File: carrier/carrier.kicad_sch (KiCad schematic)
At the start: 34 parts, among them J1 Conn_01x14, J10 Conn_02x06_Odd_Even, J2 Conn_01x14, J3 Conn_01x14, J4 Conn_01x14, J5 Conn_02x14_Odd_Even, J6 Conn_02x14_Odd_Even, J7 Conn_02x14_Odd_Even, J8 Conn_02x14_Odd_Even, J9 Conn_02x06_Odd_Even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

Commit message: Tweaks based on tnt's feedback
Wired GPIO to PMOD1
Switch 6 IOs on PMOD to attach to a header
Add GND test point
Add alignment holes for breakout
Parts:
- added J11: Conn_01x06, Connector_PinHeader_2.54mm:PinHeader_1x06_P2.54mm_Vertical, symbol Connector_Generic:Conn_01x06
- added TP1: TestPoint, TestPoint:TestPoint_Keystone_5005-5009_Compact, symbol Connector:TestPoint
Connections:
- net GND: now also TP1.1
- net GPIO: now also J9.12 (Pin_12)
- net IO0: no longer J10.11 (Pin_11)
- net IO1: no longer J10.12 (Pin_12)
- net IO2: no longer J10.9 (Pin_9)
- net IO3: no longer J10.10 (Pin_10)
- net IO4: no longer J10.7 (Pin_7)
- net IO5: no longer J10.8 (Pin_8)
- net IO6: no longer J10.5 (Pin_5)
- net VCCD2_PDM: now also J10.5 (Pin_5); no longer J9.12 (Pin_12)
- new net USR0: J10.8 (Pin_8), J11.1 (Pin_1)
- new net USR1: J10.7 (Pin_7), J11.2 (Pin_2)
- new net USR2: J10.10 (Pin_10), J11.3 (Pin_3)
- new net USR3: J10.9 (Pin_9), J11.4 (Pin_4)
- new net USR4: J10.12 (Pin_12), J11.5 (Pin_5)
- new net USR5: J10.11 (Pin_11), J11.6 (Pin_6)
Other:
- note added: "6 USER IOS TO SELECT PINS TO SEND TO ICEBREAKER"
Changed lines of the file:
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@@
     (stroke (width 0) (type default) (color 0 0 0 0))
   )
+  (text "6 USER IOS TO SELECT PINS\nTO SEND TO ICEBREAKER" (at 46.99 185.42 0)
+    (effects (font (size 1.27 1.27)) (justify left bottom))
+  )
+  (label "USR4" (at 156.21 182.88 0)
+    (effects (font (size 1.27 1.27)) (justify left bottom))
+  )
   (label "IO0" (at 99.06 139.7 90)
     (effects (font (size 1.27 1.27)) (justify left bottom))
@@
     (effects (font (size 1.27 1.27)) (justify right bottom))
   )
-  (label "IO3" (at 156.21 180.34 0)
+  (label "USR5" (at 85.09 180.34 0)
     (effects (font (size 1.27 1.27)) (justify left bottom))
   )
@@
     (effects (font (size 1.27 1.27)) (justify left bottom))
   )
-  (label "IO4" (at 123.19 177.8 180)
-    (effects (font (size 1.27 1.27)) (justify right bottom))
+  (label "USR0" (at 156.21 177.8 0)
+    (effects (font (size 1.27 1.27)) (justify left bottom))
   )
   (label "IO3" (at 91.44 139.6682 90)
@@
     (effects (font (size 1.27 1.27)) (justify left bottom))
   )
+  (label "USR3" (at 85.09 185.42 0)
+    (effects (font (size 1.27 1.27)) (justify left bottom))
+  )
   (label "~CS" (at 156.21 151.13 0)
     (effects (font (size 1.27 1.27)) (justify left bottom))
@@
     (effects (font (size 1.27 1.27)) (justify left bottom))
   )
-  (label "IO5" (at 156.21 177.8 0)
-    (effects (font (size 1.27 1.27)) (justify left bottom))
-  )
   (label "VCCD_PDM" (at 172.72 43.18 180)
     (effects (font (size 1.27 1.27)) (justify right bottom))
@@
     (effects (font (size 1.27 1.27)) (justify right bottom))
   )
+  (label "USR3" (at 123.19 180.34 180)
+    (effects (font (size 1.27 1.27)) (justify right bottom))
+  )
   (label "IO30" (at 71.12 69.9454 270)
     (effects (font (size 1.27 1.27)) (justify right bottom))
@@
     (effects (font (size 1.27 1.27)) (justify left bottom))
   )
+  (label "GPIO" (at 156.21 156.21 0)
+    (effects (font (size 1.27 1.27)) (justify left bottom))
+  )
   (label "IO10" (at 73.66 139.6682 90)
     (effects (font (size 1.27 1.27)) (justify left bottom))
   )
-  (label "IO2" (at 123.19 180.34 180)
-    (effects (font (size 1.27 1.27)) (justify right bottom))
-  )
-  (label "IO1" (at 156.21 182.88 0)
+  (label "USR1" (at 123.19 177.8 180)
+    (effects (font (size 1.27 1.27)) (justify right bottom))
+  )
+  (label "USR2" (at 156.21 180.34 0)
     (effects (font (size 1.27 1.27)) (justify left bottom))
   )
@@
     (effects (font (size 1.27 1.27)) (justify right bottom))
   )
+  (label "USR4" (at 85.09 182.88 0)
+    (effects (font (size 1.27 1.27)) (justify left bottom))
+  )
   (label "IO12" (at 68.58 139.541 90)
     (effects (font (size 1.27 1.27)) (justify left bottom))
@@
     (effects (font (size 1.27 1.27)) (justify left bottom))
   )
-  (label "IO0" (at 123.19 182.88 180)
-    (effects (font (size 1.27 1.27)) (justify right bottom))
-  )
-  (label "IO6" (at 123.19 175.26 180)
-    (effects (font (size 1.27 1.27)) (justify right bottom))
-  )
   (label "IO1" (at 96.52 139.7 90)
     (effects (font (size 1.27 1.27)) (justify left bottom))
@@
     (effects (font (size 1.27 1.27)) (justify left bottom))
   )
-  (label "VCCD2_PDM" (at 156.21 156.21 0)
-    (effects (font (size 1.27 1.27)) (justify left bottom))
+  (label "VCCD2_PDM" (at 123.19 175.26 180)
+    (effects (font (size 1.27 1.27)) (justify right bottom))
   )
   (label "D0" (at 123.19 151.13 180)
     (effects (font (size 1.27 1.27)) (justify right bottom))
   )
+  (label "USR1" (at 85.09 190.5 0)
+    (effects (font (size 1.27 1.27)) (justify left bottom))
+  )
+  (label "USR5" (at 123.19 182.88 180)
+    (effects (font (size 1.27 1.27)) (justify right bottom))
+  )
   (label "IO32" (at 76.2 69.85 270)
     (effects (font (size 1.27 1.27)) (justify right bottom))
@@
     (effects (font (size 1.27 1.27)) (justify left bottom))
   )
+  (label "USR2" (at 85.09 187.96 0)
+    (effects (font (size 1.27 1.27)) (justify left bottom))
+  )
   (label "~RST" (at 115.6018 96.52 0)
     (effects (font (size 1.27 1.27)) (justify left bottom))
@@
   )
   (label "VCCD2" (at 271.78 119.38 0)
+    (effects (font (size 1.27 1.27)) (justify left bottom))
+  )
+  (label "USR0" (at 85.09 193.04 0)
     (effects (font (size 1.27 1.27)) (justify left bottom))
   )
@@
     )
     (pin "1")
+  )
+  (symbol (lib_id "Connector_Generic:Conn_01x06") (at 80.01 187.96 180) (unit 1)
+    (in_bom yes) (on_board yes) (fields_autoplaced)
+    (property "Reference" "J11" (id 0) (at 80.01 176.53 0))
+    (property "Value" "Conn_01x06" (id 1) (at 80.01 176.53 0)
+      (effects (font (size 1.27 1.27)) hide)
+    )
+    (property "Footprint" "Connector_PinHeader_2.54mm:PinHeader_1x06_P2.54mm_Vertical" (id 2) (at 80.01 187.96 0)
+      (effects (font (size 1.27 1.27)) hide)
+    )
+    (property "Datasheet" "~" (id 3) (at 80.01 187.96 0)
+      (effects (font (size 1.27 1.27)) hide)
+    )
+    (pin "1")
+    (pin "2")
+    (pin "3")
+    (pin "4")
+    (pin "5")
+    (pin "6")
   )
   (symbol (lib_id "power:GND") (at 196.85 140.97 0) (unit 1)
@@
     (pin "5")
   )
+  (symbol (lib_id "power:GND") (at 30.48 157.48 0) (unit 1)
+    (in_bom yes) (on_board yes) (fields_autoplaced)
+    (property "Reference" "#PWR07" (id 0) (at 30.48 163.83 0)
+      (effects (font (size 1.27 1.27)) hide)
+    )
+    (property "Value" "GND" (id 1) (at 30.48 162.56 0))
+    (property "Footprint" "" (id 2) (at 30.48 157.48 0)
+      (effects (font (size 1.27 1.27)) hide)
+    )
+    (property "Datasheet" "" (id 3) (at 30.48 157.48 0)
+      (effects (font (size 1.27 1.27)) hide)
+    )
+    (pin "1")
+  )
   (symbol (lib_id "Device:R") (at 255.27 39.37 0) (unit 1)
     (in_bom yes) (on_board yes) (fields_autoplaced)
@@
     (pin "9")
   )
+  (symbol (lib_id "Connector:TestPoint") (at 30.48 157.48 0) (unit 1)
+    (in_bom yes) (on_board yes) (fields_autoplaced)
+    (property "Reference" "TP1" (id 0) (at 33.02 152.9079 0)
+      (effects (font (size 1.27 1.27)) (justify left))
+    )
+    (property "Value" "TestPoint" (id 1) (at 33.02 155.4479 0)
+      (effects (font (size 1.27 1.27)) (justify left))
+    )
+    (property "Footprint" "TestPoint:TestPoint_Keystone_5005-5009_Compact" (id 2) (at 35.56 157.48 0)
+      (effects (font (size 1.27 1.27)) hide)
+    )
+    (property "Datasheet" "~" (id 3) (at 35.56 157.48 0)
+      (effects (font (size 1.27 1.27)) hide)
+    )
+    (pin "1")
+  )
   (symbol (lib_id "Device:R") (at 255.27 95.25 0) (unit 1)
     (in_bom yes) (on_board yes) (fields_autoplaced)
@@
       (reference "#PWR06") (unit 1) (value "GND") (footprint "")
     )
+    (path "/a0ac5848-730f-422f-8f43-1a0b20d6d1cd"
+      (reference "#PWR07") (unit 1) (value "GND") (footprint "")
+    )
     (path "/c3ca63d6-04e4-444a-9ed8-3426b56704d0"
       (reference "#PWR08") (unit 1) (value "GND") (footprint "")
@@
       (reference "J10") (unit 1) (value "Conn_02x06_Odd_Even") (footprint "Connector_PinHeader_2.54mm:PinHeader_2x06_P2.54mm_Horizontal")
     )
+    (path "/6a7c960a-ea90-47ce-8d9a-a047368cb5f9"
+      (reference "J11") (unit 1) (value "Conn_01x06") (footprint "Connector_PinHeader_2.54mm:PinHeader_1x06_P2.54mm_Vertical")
+    )
     (path "/8e595552-314c-40cd-a1e4-f3727f2ff062"
       (reference "Q1") (unit 1) (value "MMBT3904") (footprint "Package_TO_SOT_SMD:SOT-23")
@@
       (reference "R12") (unit 1) (value "10K") (footprint "Resistor_SMD:R_0402_1005Metric")
     )
+    (path "/b540f9f8-84d1-47f1-a0c2-8c89eb6d4c0a"
+      (reference "TP1") (unit 1) (value "TestPoint") (footprint "TestPoint:TestPoint_Keystone_5005-5009_Compact")
+    )
     (path "/97cae384-62f8-4956-ac8e-af823a7f6b46"

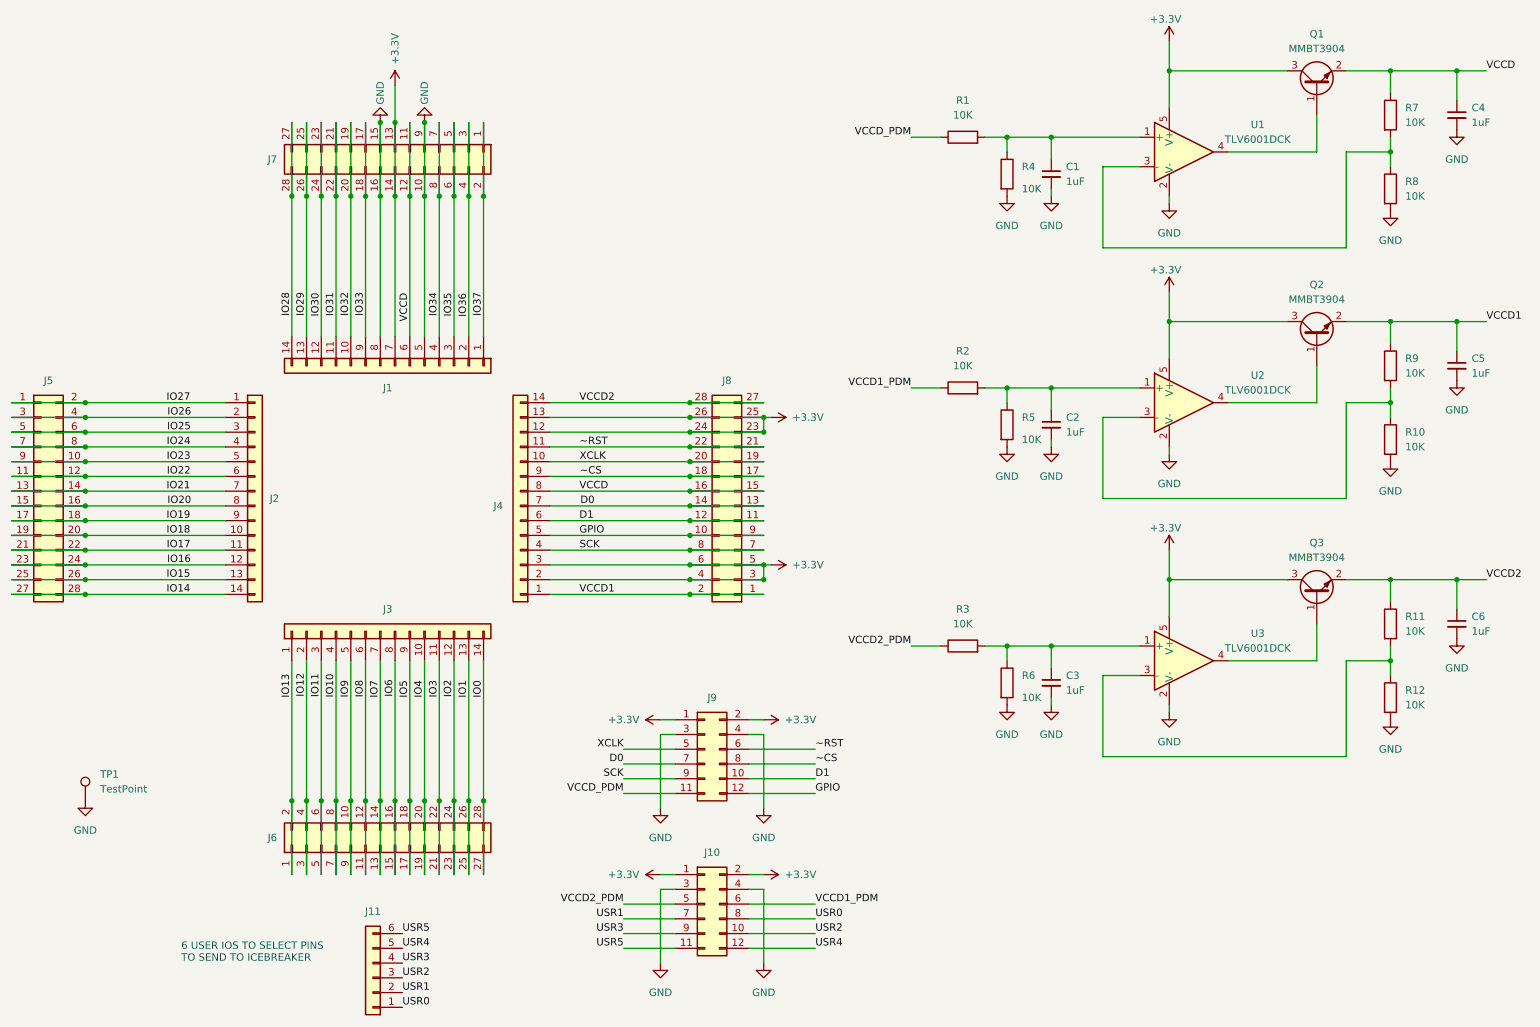
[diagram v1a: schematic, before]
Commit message: carrier: Flexy pin version
Signed-off-by: Sylvain Munaut <tnt@246tNt.com>
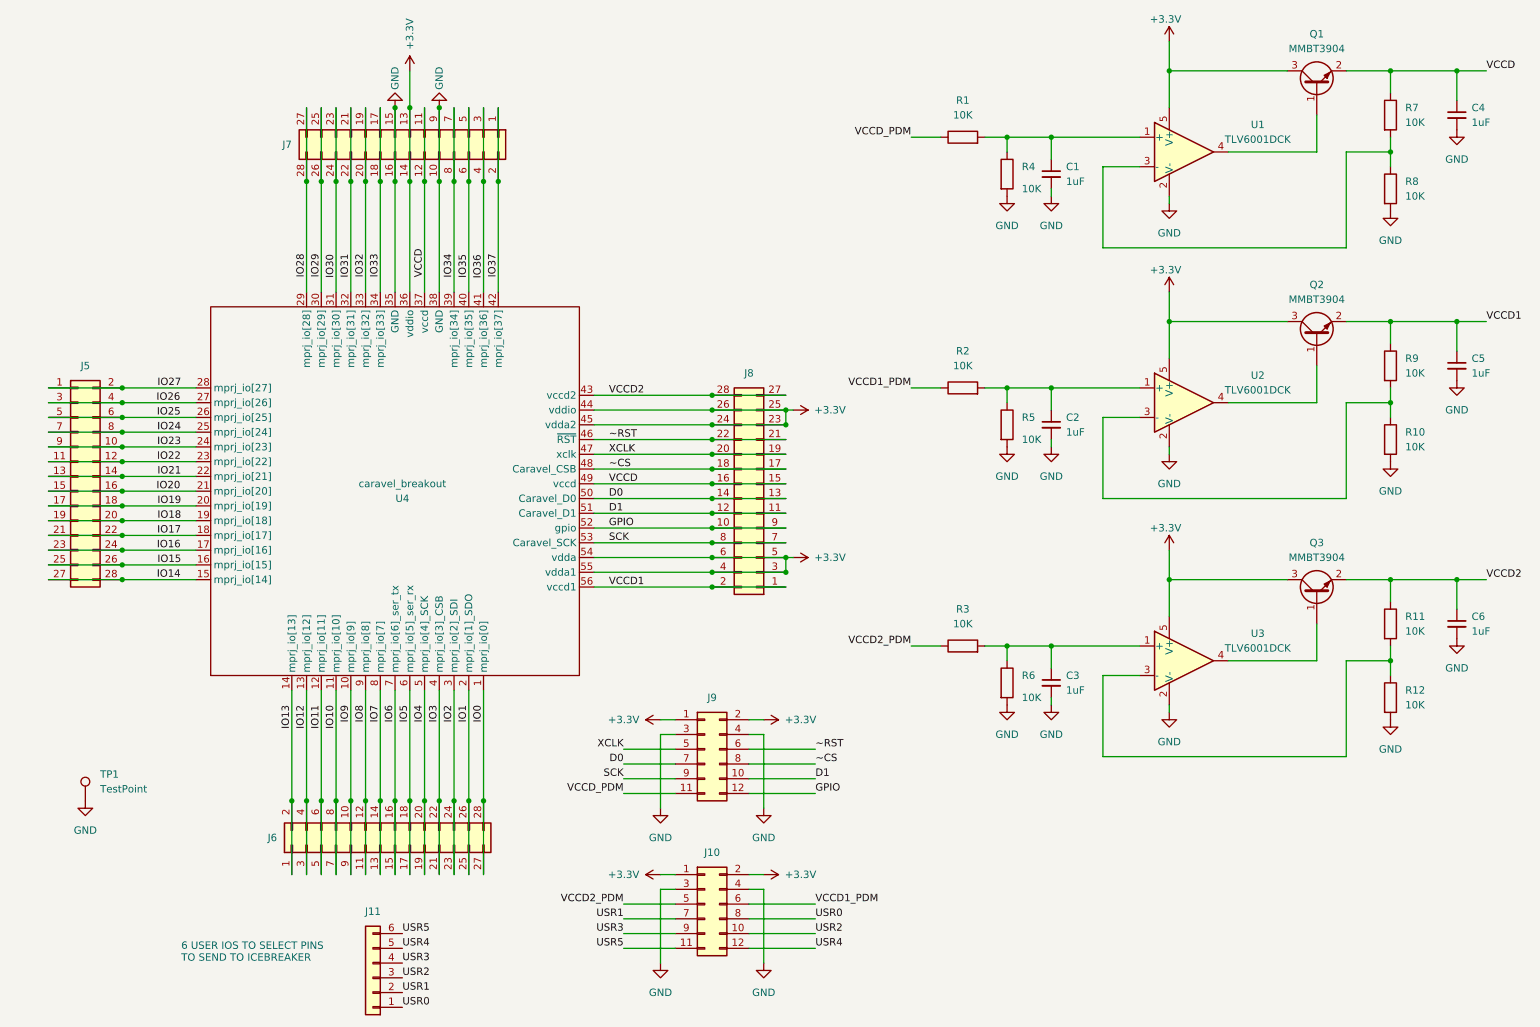
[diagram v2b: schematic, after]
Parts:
- removed J1, J2, J3, J4: Conn_01x14, Connector_PinHeader_1.27mm:PinHeader_1x14_P1.27mm_Vertical, symbol Connector_Generic:Conn_01x14
- added U4: caravel_breakout, Caravel_Board:caravel_breakout_flexy, symbol Caravel_board:caravel_breakout
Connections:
- net +3V3: now also U4.36 (vddio), U4.44 (vddio), U4.45 (vdda2), U4.54 (vdda), U4.55 (vdda1)
- net D0: now also U4.50 (Caravel_D0)
- net D1: now also U4.51 (Caravel_D1)
- net GND: now also U4.35 (GND), U4.38 (GND)
- net GPIO: now also U4.52 (gpio)
- net IO0: now also U4.1 (mprj_io[0])
- net IO1: now also U4.2 (mprj_io[1]_SDO)
- net IO10: now also U4.11 (mprj_io[10])
- net IO11: now also U4.12 (mprj_io[11])
- net IO12: now also U4.13 (mprj_io[12])
- net IO13: now also U4.14 (mprj_io[13])
- net IO14: now also U4.15 (mprj_io[14])
- net IO15: now also U4.16 (mprj_io[15])
- net IO16: now also U4.17 (mprj_io[16])
- net IO17: now also U4.18 (mprj_io[17])
- net IO18: now also U4.19 (mprj_io[18])
- net IO19: now also U4.20 (mprj_io[19])
- net IO2: now also U4.3 (mprj_io[2]_SDI)
- net IO20: now also U4.21 (mprj_io[20])
- net IO21: now also U4.22 (mprj_io[21])
- net IO22: now also U4.23 (mprj_io[22])
- net IO23: now also U4.24 (mprj_io[23])
- net IO24: now also U4.25 (mprj_io[24])
- net IO25: now also U4.26 (mprj_io[25])
- net IO26: now also U4.27 (mprj_io[26])
- net IO27: now also U4.28 (mprj_io[27])
- net IO28: now also U4.29 (mprj_io[28])
- net IO29: now also U4.30 (mprj_io[29])
- net IO3: now also U4.4 (mprj_io[3]_CSB)
- net IO30: now also U4.31 (mprj_io[30])
- net IO31: now also U4.32 (mprj_io[31])
- net IO32: now also U4.33 (mprj_io[32])
- net IO33: now also U4.34 (mprj_io[33])
- net IO34: now also U4.39 (mprj_io[34])
- net IO35: now also U4.40 (mprj_io[35])
- net IO36: now also U4.41 (mprj_io[36])
- net IO37: now also U4.42 (mprj_io[37])
- net IO4: now also U4.5 (mprj_io[4]_SCK)
- net IO5: now also U4.6 (mprj_io[5]_ser_rx)
- net IO6: now also U4.7 (mprj_io[6]_ser_tx)
- net IO7: now also U4.8 (mprj_io[7])
- net IO8: now also U4.9 (mprj_io[8])
- net IO9: now also U4.10 (mprj_io[9])
- net SCK: now also U4.53 (Caravel_SCK)
- net VCCD: now also U4.37 (vccd), U4.49 (vccd)
- net VCCD1: now also U4.56 (vccd1)
- net VCCD2: now also U4.43 (vccd2)
- net XCLK: now also U4.47 (xclk)
- net ~CS: now also U4.48 (Caravel_CSB)
- net ~RST: now also U4.46 (~{RST})
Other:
- moved on the sheet: J5, J7, J8
